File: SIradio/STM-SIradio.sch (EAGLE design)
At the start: 48 parts

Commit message: updated with v0.2 - see Readme for details
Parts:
- added LOGO1: OSHW-LOGOL, SparkFun-Aesthetics:OSHW-LOGOL
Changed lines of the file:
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@@
 <class number="1" name="vcc" width="0.381" drill="0">
+</class>
+<class number="2" name="3.3v" width="0.4064" drill="0">
 </class>
 </classes>
@@
 <part name="GND1" library="SparkFun-Aesthetics" deviceset="GND" device=""/>
 <part name="JP6" library="myconnectors" deviceset="M01" device="PTH"/>
+<part name="LOGO1" library="SparkFun-Aesthetics" deviceset="OSHW-LOGO" device="L" value="OSHW-LOGOL"/>
 </parts>
 <sheets>
@@
 <instance part="R22" gate="G$1" x="86.36" y="43.18"/>
 <instance part="SUPPLY1" gate="G$1" x="53.34" y="33.02" rot="R180"/>
-<instance part="SUPPLY2" gate="G$1" x="78.74" y="43.18" rot="R90"/>
+<instance part="SUPPLY2" gate="G$1" x="78.74" y="43.18"/>
 <instance part="JP1" gate="G$1" x="215.9" y="53.34"/>
 <instance part="JP2" gate="G$1" x="198.12" y="68.58" rot="R180"/>
@@
 <instance part="GND1" gate="1" x="137.16" y="139.7" rot="R180"/>
 <instance part="JP6" gate="G$1" x="213.36" y="81.28"/>
+<instance part="LOGO1" gate="G$1" x="218.44" y="104.14"/>
 </instances>
 <busses>

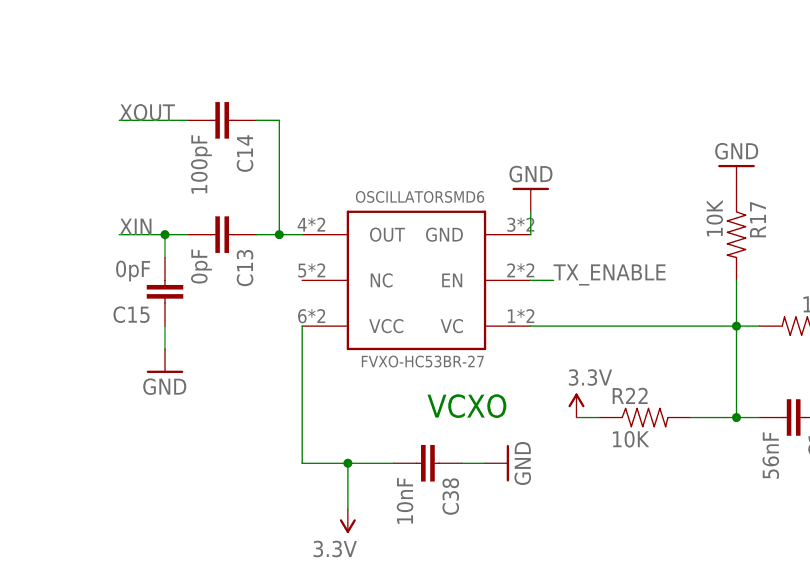
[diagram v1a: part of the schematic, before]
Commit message: Updated with new VCXO footprint, seen readme for other specifics
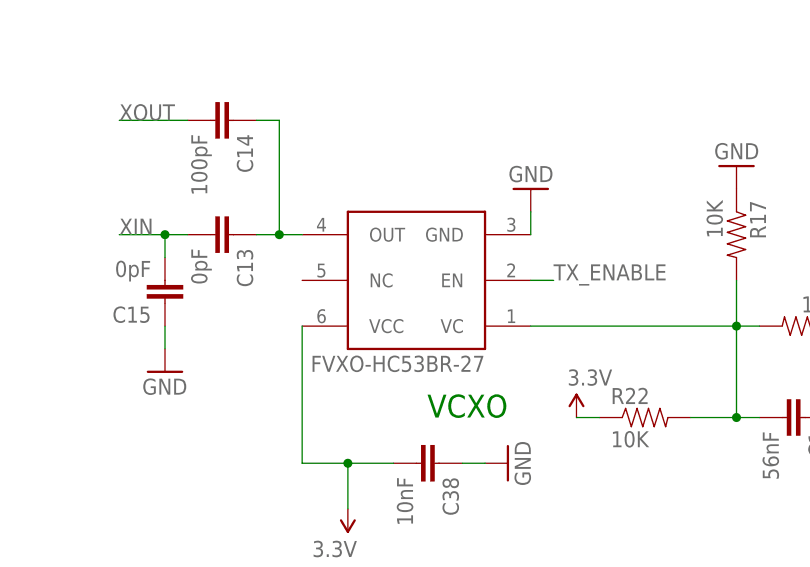
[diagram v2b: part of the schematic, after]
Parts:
- FVXO-HC53BR-27: value OSCILLATORSMD6 -> (none); device SparkFun-FreqCtrl_TK:OSCILLATORSMD6 -> SparkFun-FreqCtrl:VCXO-SMDSMD3X
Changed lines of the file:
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@@
 <part name="C38" library="SparkFun-Capacitors" deviceset="CAP" device="0603-CAP" value="10nF"/>
 <part name="GND56" library="SparkFun" deviceset="GND" device=""/>
-<part name="FVXO-HC53BR-27" library="SparkFun-FreqCtrl_TK" deviceset="OSCILLATOR" device="SMD6"/>
+<part name="FVXO-HC53BR-27" library="SparkFun-FreqCtrl" deviceset="VCXO-SMD" device="SMD3X"/>
 <part name="C13" library="SparkFun-Capacitors" deviceset="CAP" device="0603-CAP" value="0pF"/>
 <part name="C14" library="SparkFun-Capacitors" deviceset="CAP" device="0603-CAP" value="100pF"/>
@@
 <instance part="C38" gate="G$1" x="60.96" y="38.1" rot="R270"/>
 <instance part="GND56" gate="1" x="71.12" y="38.1" rot="R90"/>
-<instance part="FVXO-HC53BR-27" gate="G$1" x="60.96" y="60.96" rot="R180"/>
+<instance part="FVXO-HC53BR-27" gate="G$1" x="60.96" y="58.42" rot="R180"/>
 <instance part="C13" gate="G$1" x="38.1" y="63.5" rot="R270"/>
 <instance part="C14" gate="G$1" x="38.1" y="76.2" rot="R270"/>
@@
 <pinref part="GND29" gate="1" pin="GND"/>
 <pinref part="FVXO-HC53BR-27" gate="G$1" pin="GND"/>
-<wire x1="73.66" y1="66.04" x2="73.66" y2="63.5" width="0.1524" layer="91"/>
-</segment>
-<segment>
+<wire x1="73.66" y1="63.5" x2="73.66" y2="66.04" width="0.1524" layer="91"/>
+</segment>
+<segment>

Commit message: First Version - PCB produced
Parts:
- C18: value 0.1uF -> 100nF
- C24: value 22pf -> 22pF
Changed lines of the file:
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@@
 <part name="L8" library="SparkFun-Passives" deviceset="INDUCTOR" device="0603" value="68nH"/>
 <part name="C23" library="SparkFun-Capacitors" deviceset="CAP" device="0603-CAP" value="470pF"/>
-<part name="C24" library="SparkFun-Capacitors" deviceset="CAP" device="0603-CAP" value="22pf"/>
+<part name="C24" library="SparkFun-Capacitors" deviceset="CAP" device="0603-CAP" value="22pF"/>
 <part name="C25" library="SparkFun-Capacitors" deviceset="CAP" device="0603-CAP" value="22pF"/>
 <part name="C26" library="SparkFun-Capacitors" deviceset="CAP" device="0603-CAP" value="18pF"/>
@@
 <part name="GND29" library="SparkFun" deviceset="GND" device=""/>
 <part name="GND30" library="SparkFun" deviceset="GND" device=""/>
-<part name="C18" library="SparkFun-Capacitors" deviceset="CAP" device="0603-CAP" value="0.1uF"/>
+<part name="C18" library="SparkFun-Capacitors" deviceset="CAP" device="0603-CAP" value="100nF"/>
 <part name="C1" library="SparkFun-Capacitors" deviceset="CAP" device="0603-CAP" value="56nF"/>
 <part name="C38" library="SparkFun-Capacitors" deviceset="CAP" device="0603-CAP" value="10nF"/>
